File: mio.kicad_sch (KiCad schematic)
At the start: 8 parts, among them U201 xc7z010clg400, U701 33.3333MHz

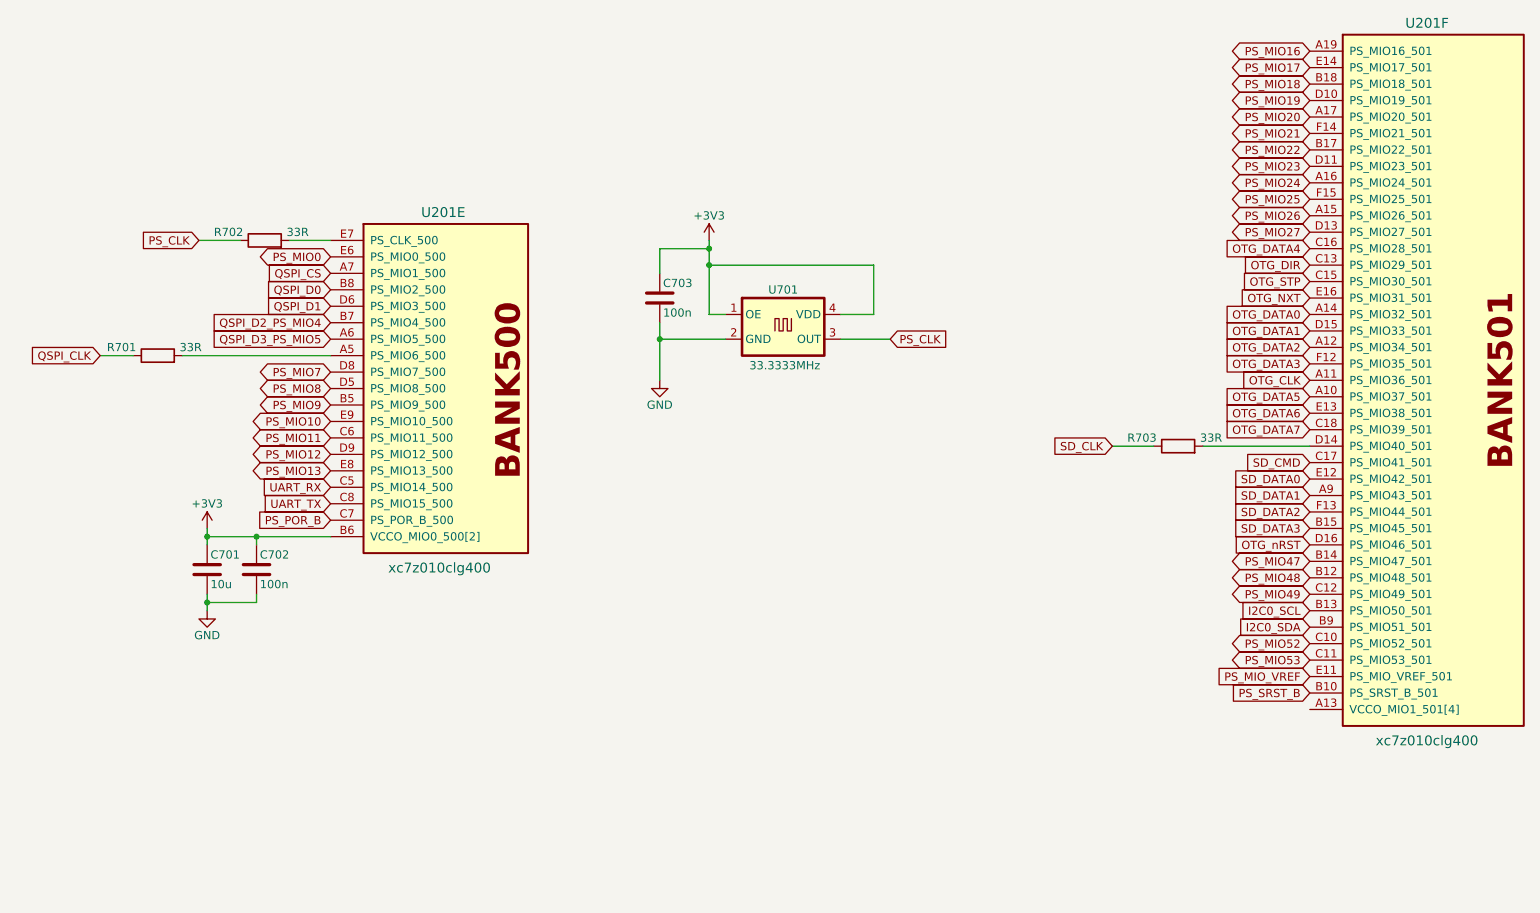
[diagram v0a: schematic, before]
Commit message: layout: routing bank 34
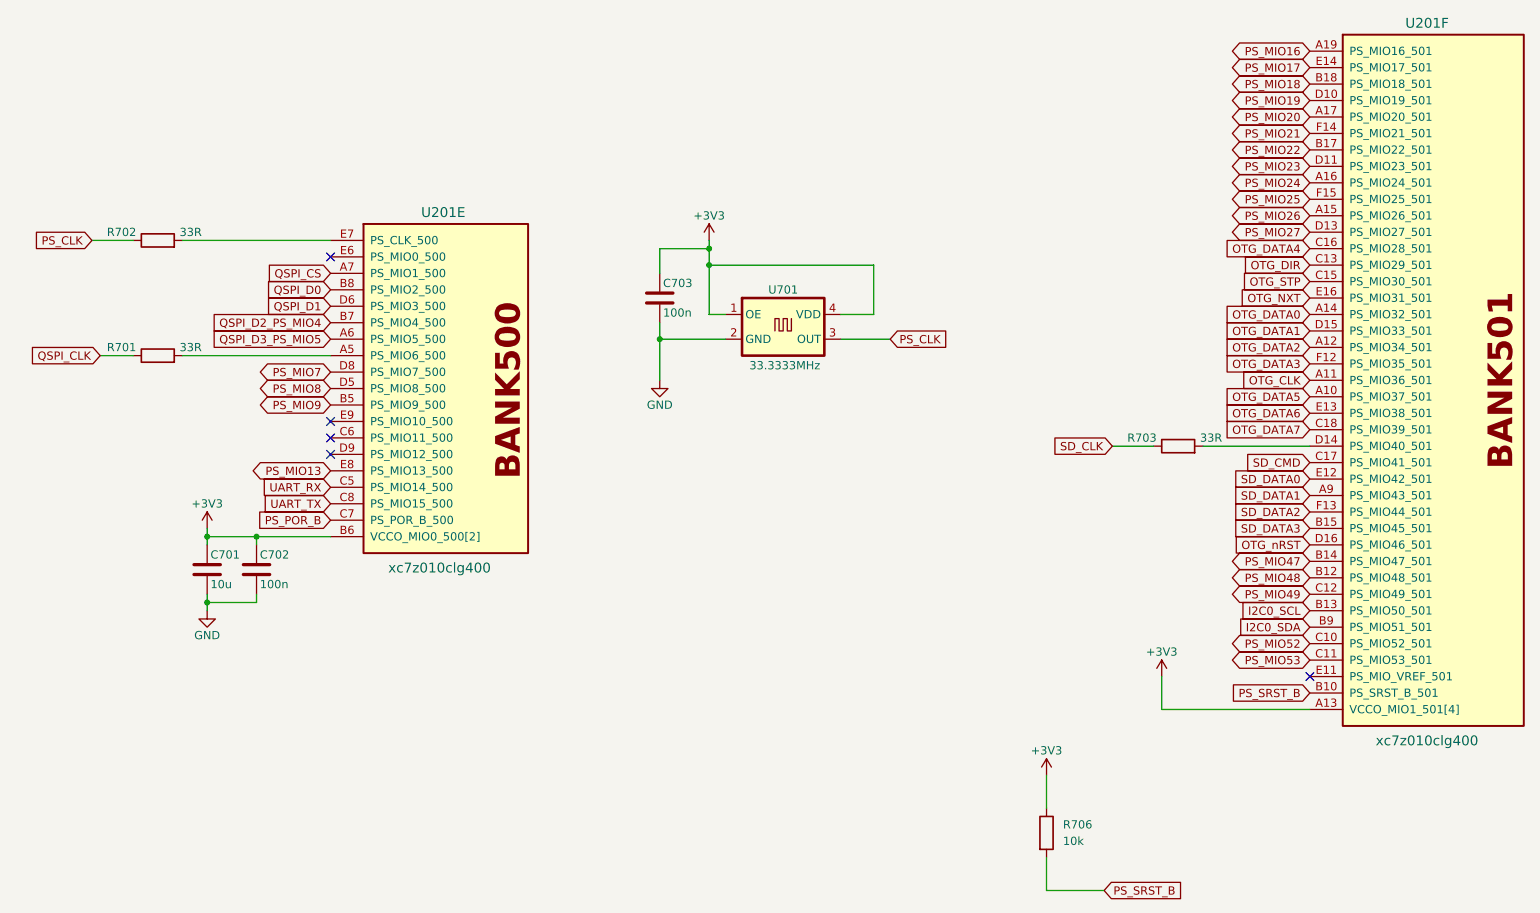
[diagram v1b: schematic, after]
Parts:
- added R706: 10k, Resistor_SMD:R_0402_1005Metric, symbol Device:R
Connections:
- net +3V3: now also U201.A13 (VCCO_MIO1_501[4]), U201.B16 (VCCO_MIO1_501[4]), U201.D12 (VCCO_MIO1_501[4]), U201.E15 (VCCO_MIO1_501[4]), R706.1
- net PS_SRST_B: now also R706.2
- net PS_MIO0: no longer names the net of U201.E6 (PS_MIO0_500)
- net PS_MIO10: no longer names the net of U201.E9 (PS_MIO10_500)
- net PS_MIO11: no longer names the net of U201.C6 (PS_MIO11_500)
- net PS_MIO12: no longer names the net of U201.D9 (PS_MIO12_500)
- net PS_MIO_VREF: no longer names the net of U201.E11 (PS_MIO_VREF_501)
- no-connect marks 0 -> 5
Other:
- moved on the sheet: R702

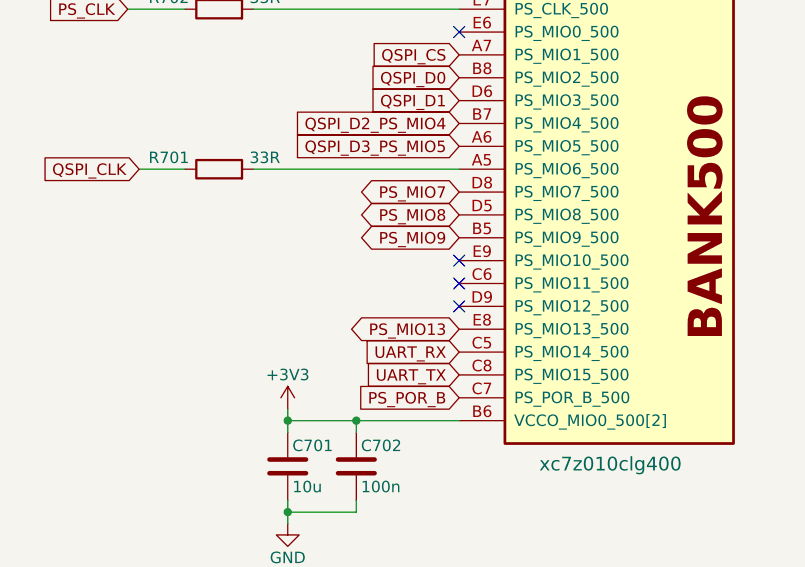
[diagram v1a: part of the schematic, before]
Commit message: layout: before rerouting ddr
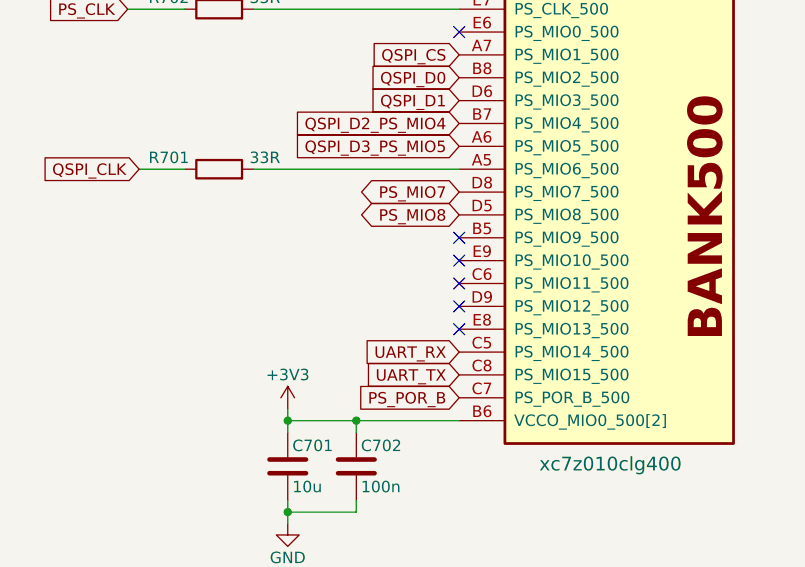
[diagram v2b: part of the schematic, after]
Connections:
- net PS_MIO13: no longer names the net of U201.E8 (PS_MIO13_500)
- net PS_MIO9: no longer names the net of U201.B5 (PS_MIO9_500)
- no-connect marks 5 -> 7
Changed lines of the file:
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@@
+	)
+	(no_connect
+		(at 74.93 81.28)
 	)
 	(no_connect
@@
 	(no_connect
 		(at 74.93 86.36)
+	)
+	(no_connect
+		(at 74.93 91.44)
 	)
 	(no_connect
@@
 		)
 	)
-	(global_label "PS_MIO9"
-		(shape bidirectional)
-		(at 74.93 81.28 180)
-		(effects
-			(font
-				(size 1.27 1.27)
-			)
-			(justify right)
-		)
-		(property "Intersheetrefs" "${INTERSHEET_REFS}"
-			(at 74.93 81.28 0)
-			(hide yes)
-			(show_name no)
-			(do_not_autoplace no)
-			(effects
-				(font
-					(size 1.27 1.27)
-				)
-			)
-		)
-	)
 	(global_label "SD_CMD"
 		(shape input)
@@
 			)
 		)
-	)
-	(global_label "PS_MIO13"
-		(shape bidirectional)
-		(at 74.93 91.44 180)
-		(effects
-			(font
-				(size 1.27 1.27)
-			)
-			(justify right)
-		)
-		(property "Intersheetrefs" "${INTERSHEET_REFS}"
-			(at 74.93 91.44 0)
-			(hide yes)
-			(show_name no)
-			(do_not_autoplace no)
-			(effects
-				(font
-					(size 1.27 1.27)
-				)
-			)
-		)
